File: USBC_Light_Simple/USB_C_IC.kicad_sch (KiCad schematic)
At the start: 20 parts, among them IC1 AP33772SDKZ-13-FA01, J1 USB_C_Receptacle, J2 Screw_Terminal_01x02

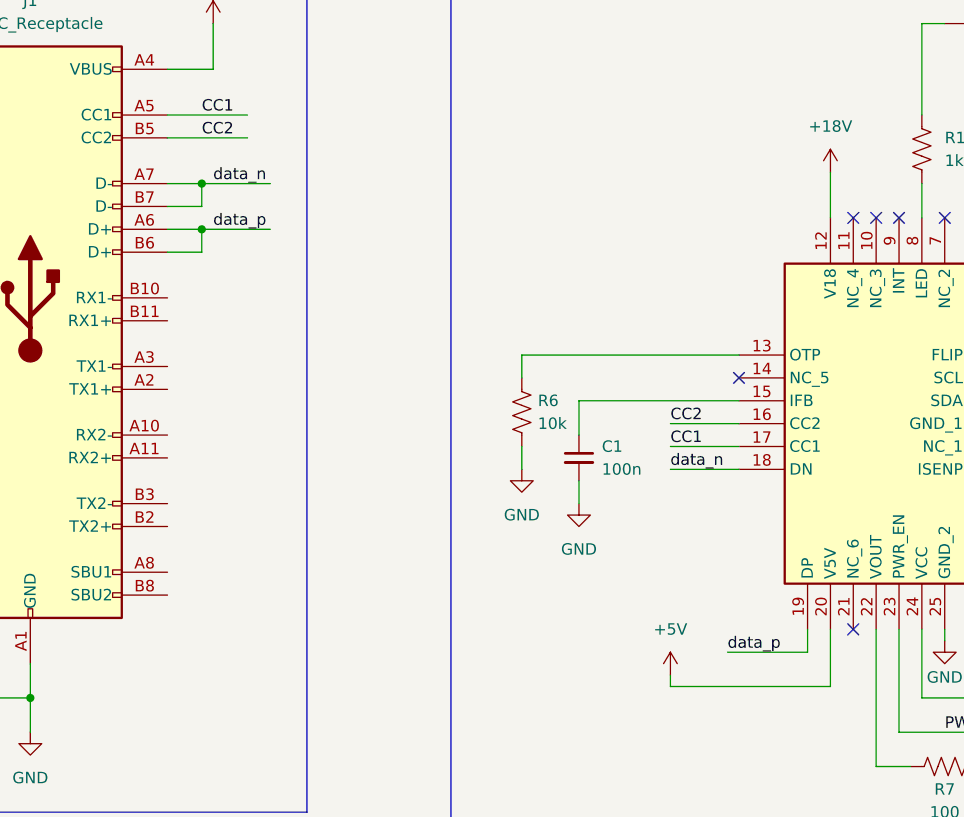
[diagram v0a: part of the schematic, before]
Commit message: Continued work:
- Added LED driver and STM32
- Began basic layout
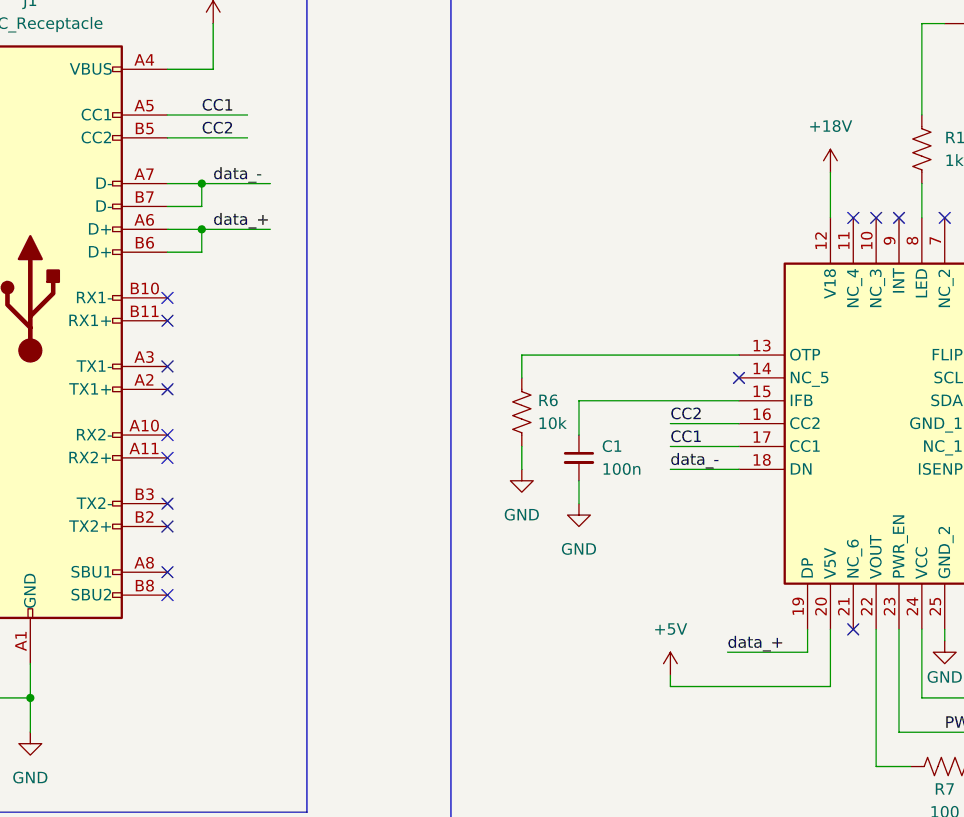
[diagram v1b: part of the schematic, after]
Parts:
- J1: footprint (none) -> USB-light-pro:CONN24_4056-03-A_GCT
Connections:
- net data_n renamed data_-
- net data_p renamed data_+
- no-connect marks 8 -> 18
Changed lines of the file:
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@@
 	)
 	(no_connect
+		(at 54.61 83.82)
+	)
+	(no_connect
+		(at 54.61 78.74)
+	)
+	(no_connect
+		(at 54.61 68.58)
+	)
+	(no_connect
+		(at 54.61 76.2)
+	)
+	(no_connect
 		(at 130.81 105.41)
 	)
@@
 	)
 	(no_connect
+		(at 54.61 101.6)
+	)
+	(no_connect
 		(at 135.89 59.69)
 	)
 	(no_connect
+		(at 54.61 86.36)
+	)
+	(no_connect
+		(at 54.61 91.44)
+	)
+	(no_connect
 		(at 148.59 85.09)
 	)
 	(no_connect
+		(at 54.61 99.06)
+	)
+	(no_connect
 		(at 118.11 77.47)
 	)
+	(no_connect
+		(at 54.61 93.98)
+	)
+	(no_connect
+		(at 54.61 71.12)
+	)
 	(wire
 		(pts
@@
 		)
 	)
-	(label "data_n"
+	(label "data_-"
 		(at 59.69 55.88 0)
 		(effects
@@
 		)
 	)
-	(label "data_p"
+	(label "data_+"
 		(at 59.69 60.96 0)
 		(effects
@@
 		)
 	)
-	(label "data_n"
+	(label "data_-"
 		(at 110.49 87.63 0)
 		(effects
@@
 		)
 	)
-	(label "data_p"
+	(label "data_+"
 		(at 116.84 107.95 0)
 		(effects
@@
 			)
 		)
-		(property "Footprint" ""
+		(property "Footprint" "USB-light-pro:CONN24_4056-03-A_GCT"
 			(at 43.18 68.58 0)
 			(effects

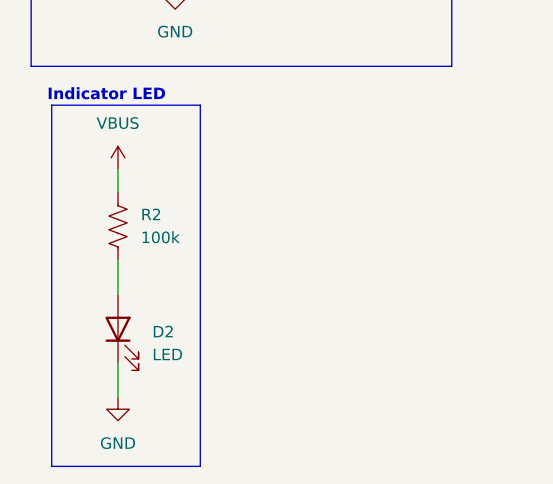
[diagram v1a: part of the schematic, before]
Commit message: Preliminary component placement on board.
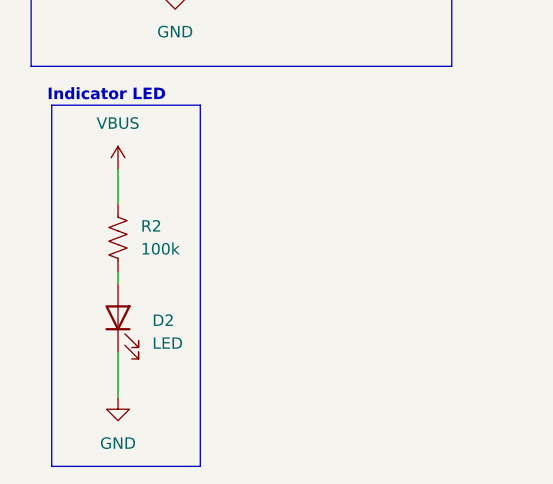
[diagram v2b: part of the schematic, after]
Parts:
- C1, C10, C2, C3, C4, C5, C6, C7, C8, C9: footprint (none) -> Capacitor_SMD:C_0603_1608Metric_Pad1.08x0.95mm_HandSolder
- D1, D2: footprint (none) -> LED_SMD:LED_0603_1608Metric_Pad1.05x0.95mm_HandSolder
- R1, R2, R6, R7: footprint (none) -> Resistor_SMD:R_0603_1608Metric_Pad0.98x0.95mm_HandSolder
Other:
- moved on the sheet: D2, R2
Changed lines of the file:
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@@
 	(wire
 		(pts
-			(xy 33.02 137.16) (xy 33.02 139.7)
+			(xy 33.02 137.16) (xy 33.02 140.97)
 		)
 		(stroke
@@
 	(wire
 		(pts
-			(xy 33.02 147.32) (xy 33.02 151.13)
+			(xy 33.02 148.59) (xy 33.02 149.86)
 		)
 		(stroke
@@
 	(wire
 		(pts
-			(xy 33.02 158.75) (xy 33.02 162.56)
+			(xy 33.02 157.48) (xy 33.02 162.56)
 		)
 		(stroke
@@
 			)
 		)
-		(property "Footprint" ""
+		(property "Footprint" "Capacitor_SMD:C_0603_1608Metric_Pad1.08x0.95mm_HandSolder"
 			(at 210.82 44.45 0)
 			(effects
@@
 			)
 		)
-		(property "Footprint" ""
+		(property "Footprint" "Resistor_SMD:R_0603_1608Metric_Pad0.98x0.95mm_HandSolder"
 			(at 94.996 81.534 90)
 			(effects
@@
 			)
 		)
-		(property "Footprint" ""
+		(property "Footprint" "Capacitor_SMD:C_0603_1608Metric_Pad1.08x0.95mm_HandSolder"
 			(at 190.5 44.45 0)
 			(effects
@@
 			)
 		)
-		(property "Footprint" ""
+		(property "Footprint" "Capacitor_SMD:C_0603_1608Metric_Pad1.08x0.95mm_HandSolder"
 			(at 219.71 72.39 0)
 			(effects
@@
 			)
 		)
-		(property "Footprint" ""
+		(property "Footprint" "Capacitor_SMD:C_0603_1608Metric_Pad1.08x0.95mm_HandSolder"
 			(at 241.3 44.45 0)
 			(effects
@@
 	(symbol
 		(lib_id "Device:R_US")
-		(at 33.02 143.51 0)
+		(at 33.02 144.78 0)
 		(unit 1)
 		(exclude_from_sim no)
@@
 		(fields_autoplaced yes)
 		(property "Reference" "R2"
-			(at 35.56 142.2399 0)
+			(at 35.56 143.5099 0)
 			(effects
 				(font
@@
 		)
 		(property "Value" "100k"
-			(at 35.56 144.7799 0)
+			(at 35.56 146.0499 0)
 			(effects
 				(font
@@
 			)
 		)
-		(property "Footprint" ""
-			(at 34.036 143.764 90)
+		(property "Footprint" "Resistor_SMD:R_0603_1608Metric_Pad0.98x0.95mm_HandSolder"
+			(at 34.036 145.034 90)
 			(effects
 				(font
@@
 		)
 		(property "Datasheet" "~"
-			(at 33.02 143.51 0)
+			(at 33.02 144.78 0)
 			(effects
 				(font
@@
 		)
 		(property "Description" "Resistor, US symbol"
-			(at 33.02 143.51 0)
+			(at 33.02 144.78 0)
 			(effects
 				(font
@@
 			)
 		)
-		(property "Footprint" ""
+		(property "Footprint" "LED_SMD:LED_0603_1608Metric_Pad1.05x0.95mm_HandSolder"
 			(at 144.78 38.1 0)
 			(effects
@@
 			)
 		)
-		(property "Footprint" ""
+		(property "Footprint" "Resistor_SMD:R_0603_1608Metric_Pad0.98x0.95mm_HandSolder"
 			(at 140.716 121.666 90)
 			(effects
@@
 			)
 		)
-		(property "Footprint" ""
+		(property "Footprint" "Resistor_SMD:R_0603_1608Metric_Pad0.98x0.95mm_HandSolder"
 			(at 139.446 52.324 90)
 			(effects
@@
 			)
 		)
-		(property "Footprint" ""
+		(property "Footprint" "Capacitor_SMD:C_0603_1608Metric_Pad1.08x0.95mm_HandSolder"
 			(at 200.66 44.45 0)
 			(effects
@@
 	(symbol
 		(lib_id "Device:LED")
-		(at 33.02 154.94 90)
+		(at 33.02 153.67 90)
 		(unit 1)
 		(exclude_from_sim no)
@@
 		(fields_autoplaced yes)
 		(property "Reference" "D2"
-			(at 36.83 155.2574 90)
+			(at 36.83 153.9874 90)
 			(effects
 				(font
@@
 		)
 		(property "Value" "LED"
-			(at 36.83 157.7974 90)
+			(at 36.83 156.5274 90)
 			(effects
 				(font
@@
 			)
 		)
-		(property "Footprint" ""
-			(at 33.02 154.94 0)
+		(property "Footprint" "LED_SMD:LED_0603_1608Metric_Pad1.05x0.95mm_HandSolder"
+			(at 33.02 153.67 0)
 			(effects
 				(font
@@
 		)
 		(property "Datasheet" "~"
-			(at 33.02 154.94 0)
+			(at 33.02 153.67 0)
 			(effects
 				(font
@@
 		)
 		(property "Description" "Light emitting diode"
-			(at 33.02 154.94 0)
+			(at 33.02 153.67 0)
 			(effects
 				(font
@@
 		)
 		(property "Sim.Pins" "1=K 2=A"
-			(at 33.02 154.94 0)
+			(at 33.02 153.67 0)
 			(effects
 				(font
@@
 			)
 		)
-		(property "Footprint" ""
+		(property "Footprint" "Capacitor_SMD:C_0603_1608Metric_Pad1.08x0.95mm_HandSolder"
 			(at 257.81 44.45 0)
 			(effects
@@
 			)
 		)
-		(property "Footprint" ""
+		(property "Footprint" "Capacitor_SMD:C_0603_1608Metric_Pad1.08x0.95mm_HandSolder"
 			(at 231.14 44.45 0)
 			(effects
@@
 			)
 		)
-		(property "Footprint" ""
+		(property "Footprint" "Capacitor_SMD:C_0603_1608Metric_Pad1.08x0.95mm_HandSolder"
 			(at 229.87 72.39 0)
 			(effects
@@
 			)
 		)
-		(property "Footprint" ""
+		(property "Footprint" "Capacitor_SMD:C_0603_1608Metric_Pad1.08x0.95mm_HandSolder"
 			(at 100.33 86.36 0)
 			(effects
@@
 			)
 		)
-		(property "Footprint" ""
+		(property "Footprint" "Capacitor_SMD:C_0603_1608Metric_Pad1.08x0.95mm_HandSolder"
 			(at 209.55 72.39 0)
 			(effects
